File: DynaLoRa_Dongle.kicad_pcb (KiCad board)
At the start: 2 copper layers, 62.2 x 16.6 mm, 32 parts, among them J1 Conn_01x07, J2 USB_A, J3 Conn_Coaxial, J4 Micro_SD_Card, SW1 SW_Push, SW2 SW_Push, U1 GD25Q32, U2 ATSAMD21E18A-AUT, U3 RFM9X, U4 SY80XX

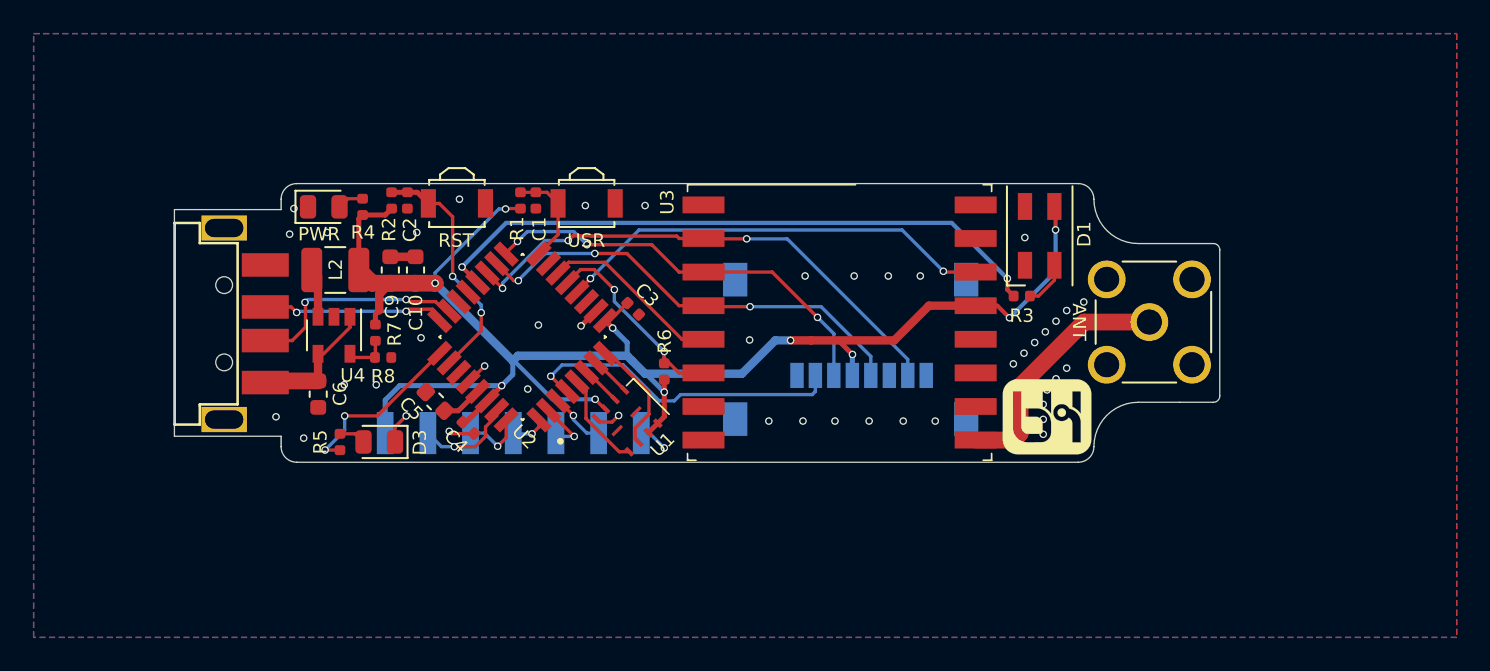
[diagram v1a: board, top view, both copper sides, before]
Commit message: v3 changes
- Use standard 2.54 mm vertical THT pin header! (finally)
- Replace buttons for bigger ones that are easier to press (the same ones as DynOSSAT-EDU)
- Replace DC/DC for a 500 mA LDO to simplify assembly, since USB won't source more than 500 mA anyway
- The ATSAMD21E18 is now the QFN version instead of QFP
- Replace pin naming on the header by their Arduino/CircuitPython naming (i.e. PA00 is now D0, etc)

It should be fully compatible with the v2, no software changes needed.
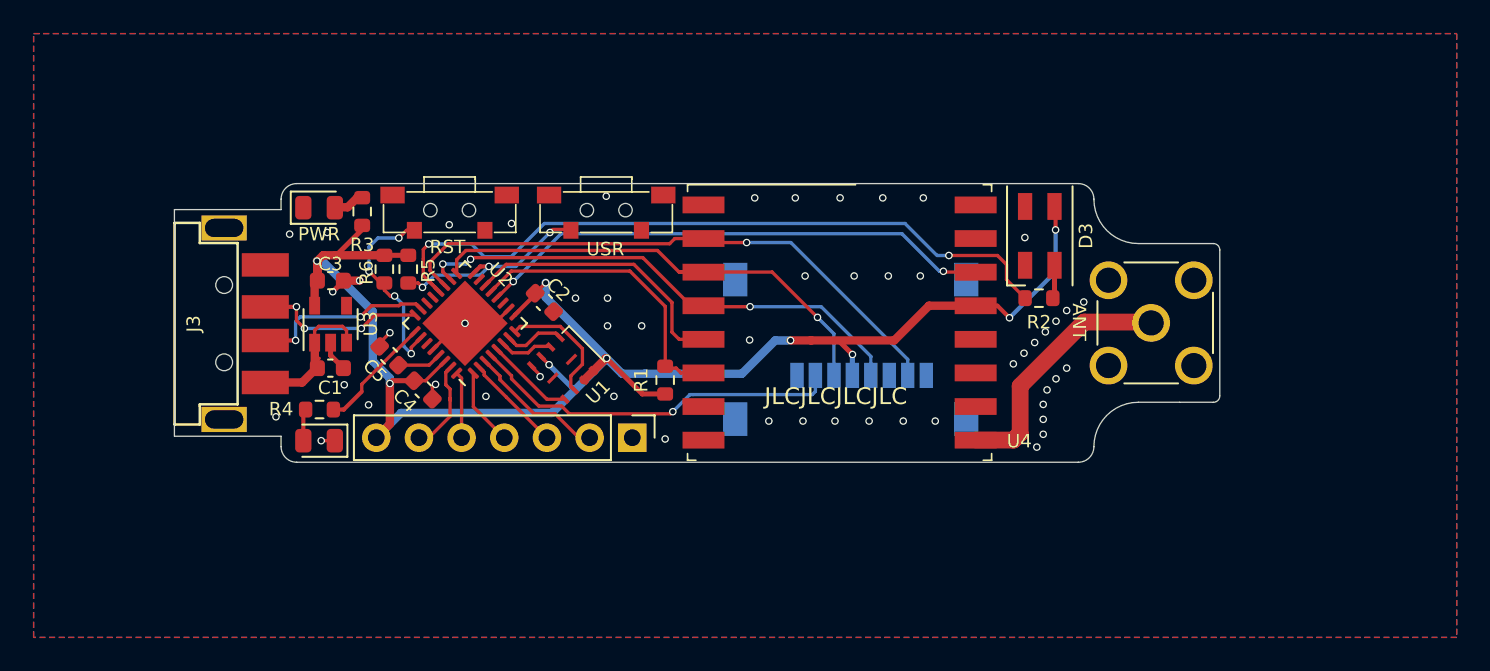
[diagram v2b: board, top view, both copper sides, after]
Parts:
- removed C10, C6, C9: 22uF, Capacitor_SMD:C_0603_1608Metric
- removed the G*** at (34.4, -60.5)
- removed the G*** at (68.2, -51.6)
- removed L2: 2.2uH, Inductor_SMD:L_1210_3225Metric
- removed R7: 100k, Resistor_SMD:R_0402_1005Metric
- removed R8: 22k, Resistor_SMD:R_0402_1005Metric
- added G***: LOGO, DynOSSAT:logo_full_small, B.Cu at (35.9, -59.9)
- added G***: LOGO, DynOSSAT:freq_selector, B.Cu at (21.6, -57.2)
- C1: value 10nF -> 22uF; footprint Capacitor_SMD:C_0402_1005Metric -> Capacitor_SMD:C_0603_1608Metric
- C2: value 10nF -> 100nF; footprint Capacitor_SMD:C_0402_1005Metric -> Capacitor_SMD:C_0603_1608Metric
- C3: value 100nF -> 22uF; footprint Capacitor_SMD:C_0402_1005Metric -> Capacitor_SMD:C_0603_1608Metric
- C4: footprint Capacitor_SMD:C_0402_1005Metric -> Capacitor_SMD:C_0603_1608Metric
- D1: value WS2812B -> LED_Small; footprint DynOSSAT:LED_SK6812MINI_PLCC4_3.5x3.5mm_P1.75mm -> LED_SMD:LED_0805_2012Metric
- D3: value LED_Small -> WS2812B; footprint LED_SMD:LED_0805_2012Metric -> DynOSSAT:LED_SK6812MINI_PLCC4_3.5x3.5mm_P1.75mm
- J1: footprint DynOSSAT:PinHeader_1x07_P2.54mm_Vertical_SMD_Pin1Left -> Connector_PinHeader_2.54mm:PinHeader_1x07_P2.54mm_Vertical; moved to F.Cu
- J2: value USB_A -> Conn_Coaxial; footprint DynOSSAT:C46394 -> Connector_Coaxial:SMA_Molex_73251-2200_Horizontal
- J3: value Conn_Coaxial -> USB_A; footprint Connector_Coaxial:SMA_Molex_73251-2200_Horizontal -> DynOSSAT:C46394
- R1, R3, R4, R6: footprint Resistor_SMD:R_0402_1005Metric -> Resistor_SMD:R_0603_1608Metric
- R2: value 100k -> 510R; footprint Resistor_SMD:R_0402_1005Metric -> Resistor_SMD:R_0603_1608Metric
- R5: value 510R -> 100k; footprint Resistor_SMD:R_0402_1005Metric -> Resistor_SMD:R_0603_1608Metric
- SW1, SW2: footprint DynOSSAT:SW_SPST_B3U-3000P -> DynOSSAT:1TS002G-1800-3500-CT
- U2: footprint DynOSSAT:QFP80P900X900X120-32N -> Package_DFN_QFN:QFN-32-1EP_5x5mm_P0.5mm_EP3.6x3.6mm
- U3: value RFM9X -> ME6211C; footprint DynOSSAT:HOPERF_RFM69HW -> Package_TO_SOT_SMD:SOT-23-5
- U4: value SY80XX -> RFM9X; footprint Package_TO_SOT_SMD:SOT-23-5 -> DynOSSAT:HOPERF_RFM69HW
- moved J2 58.1 mm to (74.4, -57.2), turned to 270 degrees
- moved J3 58.0 mm to (16.3, -57.5), turned to 90 degrees
- moved D1 42.9 mm to (24.9, -64.1), turned to 0 degrees
- moved D3 41.2 mm to (67.8, -62.4), turned to 270 degrees
- moved R3 39.6 mm to (27.4, -63.8), turned to 90 degrees
- moved R2 39.0 mm to (67.7, -58.7), turned to 180 degrees
- moved U3 30.3 mm to (25.6, -57.1), turned to 90 degrees
- moved U4 30.1 mm to (55.8, -57.2), turned to 0 degrees
- moved C3 18.1 mm to (25.5, -59.7), turned to 0 degrees
- moved R6 17.7 mm to (28.8, -60.4), turned to 270 degrees
- moved C1 15.8 mm to (25.5, -54.5), turned to 0 degrees
- moved D2 13.9 mm to (24.9, -50.2), turned to 180 degrees
- moved R1 13.7 mm to (45.5, -53.8)
- moved R4 12.3 mm to (24.9, -52.0), turned to 180 degrees
- moved R5 11.1 mm to (30.2, -60.4), turned to 270 degrees
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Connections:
- C1 pad 1: /USER_BTN -> VBUS
- C2 pad 1: /nRESET -> +3V3
- D1 pad 1: +3V3 -> GND
- D3 pad 1: GND -> +3V3
- J2 pad 1: VBUS -> Net-(J2-Pad1)
- J2 pad 2: USB_D- -> GND
- J3 pad 1: Net-(J3-Pad1) -> VBUS
- J3 pad 2: GND -> USB_D-
- R1 pad 2: /USER_BTN -> /RF_RESET
- R2 pad 1: +3V3 -> Net-(D3-Pad4)
- R2 pad 2: /nRESET -> /RGB
- R3 pad 1: Net-(D1-Pad4) -> +3V3
- R3 pad 2: /RGB -> Net-(D1-Pad2)
- R4 pad 1: +3V3 -> /LED
- R5 pad 1: /LED -> +3V3
- R5 pad 2: Net-(D3-Pad2) -> /USER_BTN
- R6 pad 2: /RF_RESET -> /nRESET
- SW1 pad 1: /USER_BTN -> GND
- SW1 pad 2: GND -> /USER_BTN
- SW2 pad 1: /nRESET -> GND
- SW2 pad 2: GND -> /nRESET
- U3 pad 1: GND -> VBUS
- U3 pad 2: /SDI -> GND
- U3 pad 3: /SDO -> VBUS
- U3 pad 4: /SCK -> Net-(U3-Pad4)
- U3 pad 5: /RF_CS -> +3V3
- U4 pad 1: VBUS -> GND
- U4 pad 2: GND -> /SDI
- U4 pad 3: Net-(L2-Pad1) -> /SDO
- U4 pad 4: VBUS -> /SCK
- U4 pad 5: Net-(R7-Pad2) -> /RF_CS
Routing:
- net Net-(J3-Pad1): track 14.9 -> 0.00 mm
- net Net-(J2-Pad1): track 0.00 -> 14.9 mm
- net /RGB: track 37.4 -> 43.2 mm
- net /USER_BTN: track 6.54 -> 12.3 mm, vias 0 -> 3
- net /RF_CS: track 10.8 -> 16.4 mm
- net /RF_RESET: track 12.3 -> 17.7 mm, vias 2 -> 0
- net /PA02: track 3.35 -> 8.22 mm, vias 1 -> 0
- net /RF_INT: track 26.3 -> 31.0 mm
- net /SDO: track 25.1 -> 29.5 mm, vias 3 -> 1
- net /SDI: track 31.0 -> 34.7 mm, vias 3 -> 1
- net /LED: track 10.6 -> 7.05 mm, vias 2 -> 0
- net /SCK: track 27.0 -> 30.3 mm
- net Net-(L2-Pad1): track 2.94 -> 0.00 mm
- net Net-(D3-Pad4): track 0.00 -> 2.89 mm
- net /SD_CS: track 19.5 -> 22.3 mm
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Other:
- board text added: "D0"
- board text added: "D1"
- board text added: "D3"
- board text added: "D4"
- board text added: "JLCJLCJLCJLC"
- board text added: "USB Dongle v3"
- board text added: "~~D2"
- board text removed: "PA00"
- board text removed: "PA01"
- board text removed: "PA02"
- board text removed: "SWCLK"
- board text removed: "SWDIO"
- board text removed: "USB Dongle v2"
